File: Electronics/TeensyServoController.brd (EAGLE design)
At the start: 50.8 x 38.1 mm, 96 parts, among them U1 TEENSY_3.1_ALLPINS, U12 MIC5225, U13 MIC5225, U2 AP3211KTR-G1, U3 AP3211KTR-G1, U4 AP3211KTR-G1, U5 AP2210N-3.3TRG1

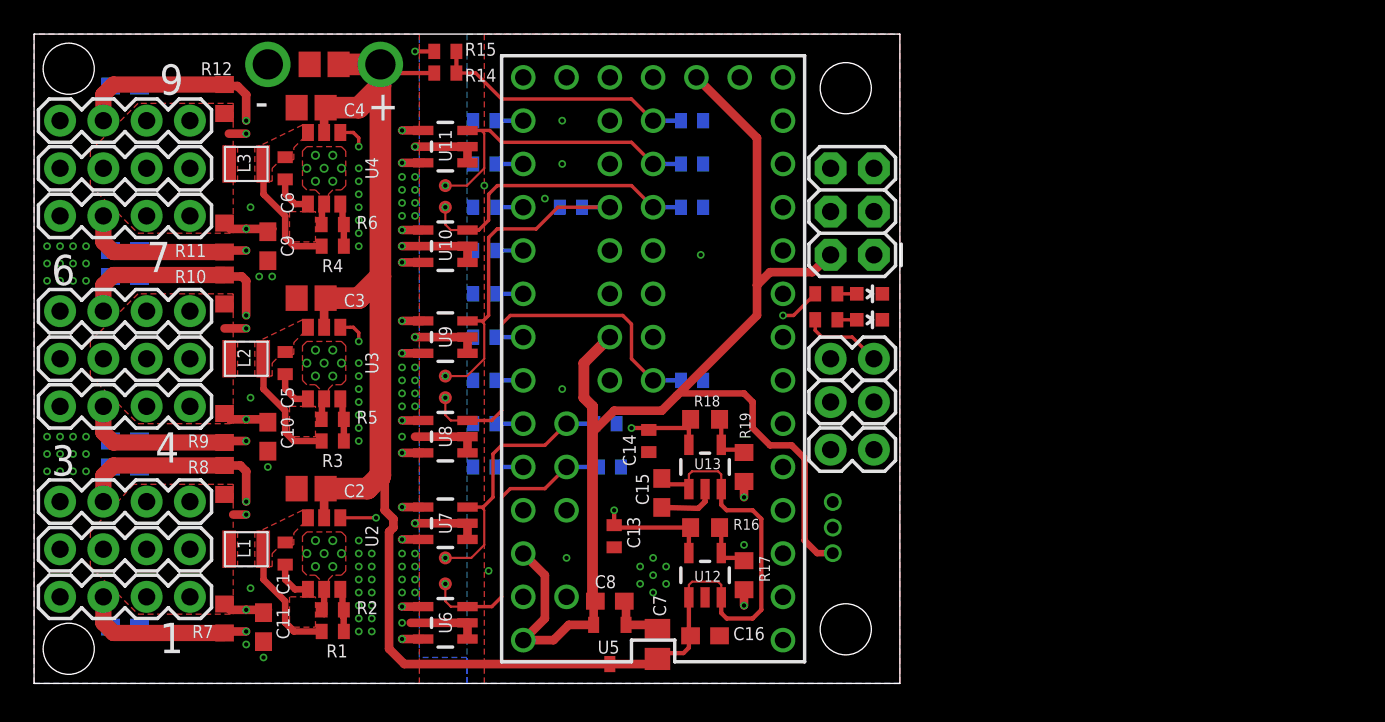
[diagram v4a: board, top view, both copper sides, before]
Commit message: Updated PCB design after receiving rev 1
Fixed regulator footprint
Changed a few part packages
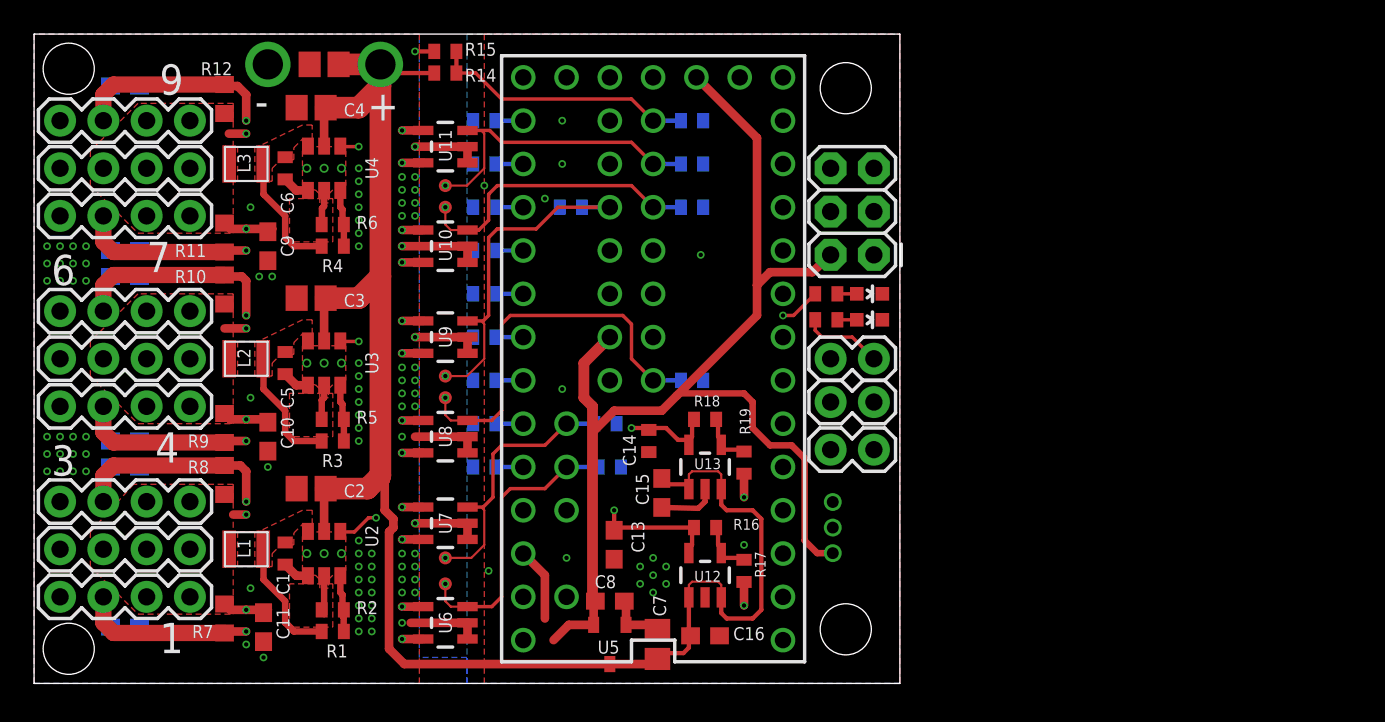
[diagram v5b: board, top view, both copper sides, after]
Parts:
- C12: value 10uF -> 22uF
- C13: value 0.1uF -> 1uF; device resistor:C0402 -> resistor:C0603
- C16, C8: value 0.1uF -> 1uF
- R16, R17, R18, R19: device resistor:R0603 -> resistor:R0402
- moved C13 0.50 mm to (34.0, 8.14)
- moved R19 0.25 mm to (41.7, 13.0)
- moved R17 0.25 mm to (41.7, 6.60)
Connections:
- new net VIN: U1.VIN
- net VDD: no longer U1.VIN
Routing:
- net SERVO_VDD-2: track 26.9 -> 18.7 mm
- net VDD: track 92.3 -> 88.7 mm
- net GND: track 39.6 -> 42.9 mm, vias 131 -> 119
- net VCC: track 101.7 -> 104.1 mm
- net N$14: track 2.45 -> 1.61 mm
- net N$17: track 2.45 -> 1.61 mm
- net N$19: track 2.45 -> 1.61 mm
- net N$6: track 3.26 -> 4.06 mm
- net N$18: track 2.56 -> 3.36 mm
- net N$16: track 2.56 -> 3.36 mm
- net EN-2: track 26.2 -> 25.6 mm
- net EN-3: track 22.5 -> 21.9 mm
- net AREF: track 9.75 -> 10.3 mm

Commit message: Increased PCB CAD model detail
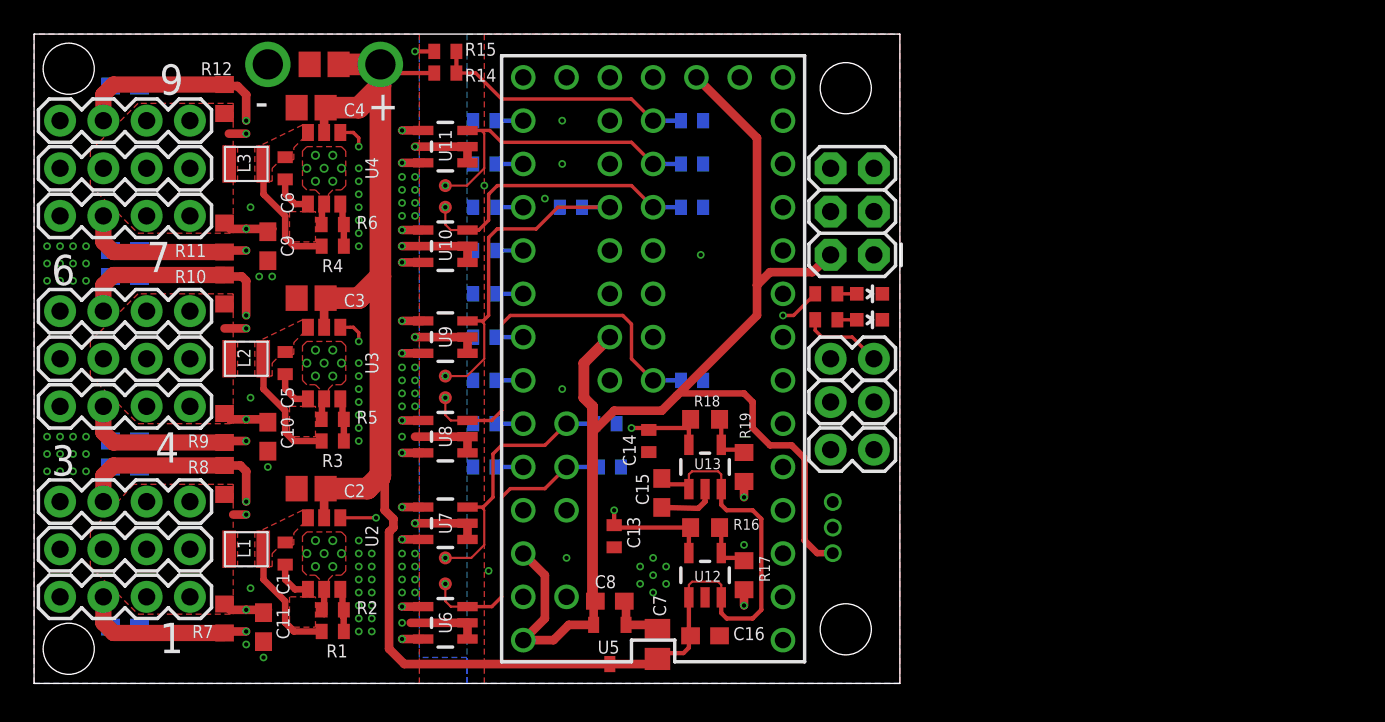
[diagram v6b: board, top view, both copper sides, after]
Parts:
- C12: value 22uF -> 10uF
- C13: value 1uF -> 0.1uF; device resistor:C0603 -> resistor:C0402
- C16, C8: value 1uF -> 0.1uF
- R16, R17, R18, R19: device resistor:R0402 -> resistor:R0603
- moved C13 0.50 mm to (34.0, 8.64)
- moved R19 0.25 mm to (41.7, 12.7)
- moved R17 0.25 mm to (41.7, 6.35)
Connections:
- removed net VIN: U1.VIN
- net VDD: now also U1.VIN
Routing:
- net SERVO_VDD-2: track 18.7 -> 26.9 mm
- net VDD: track 88.7 -> 92.3 mm
- net GND: track 42.9 -> 39.6 mm, vias 119 -> 131
- net VCC: track 104.1 -> 101.7 mm
- net N$14: track 1.61 -> 2.45 mm
- net N$17: track 1.61 -> 2.45 mm
- net N$19: track 1.61 -> 2.45 mm
- net N$6: track 4.06 -> 3.26 mm
- net N$18: track 3.36 -> 2.56 mm
- net N$16: track 3.36 -> 2.56 mm
- net EN-2: track 25.6 -> 26.2 mm
- net EN-3: track 21.9 -> 22.5 mm
- net AREF: track 10.3 -> 9.75 mm
